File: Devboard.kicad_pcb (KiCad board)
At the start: 4 copper layers, 33.7 x 50.4 mm, 40 parts, among them J1 USB_C_Receptacle_USB2.0_14P, J2 Conn_01x03, J3 Conn_01x10, J4 Conn_01x10, J5 JST_2mm_LiPo, J6 Conn_01x10, J7 Conn_01x10, SW1 SW_Push, U1 RP2040, U2 NCP1117-3.3_SOT223, U3 W25Q128JVS, U4 MPU-9250, Y1 12Mhz

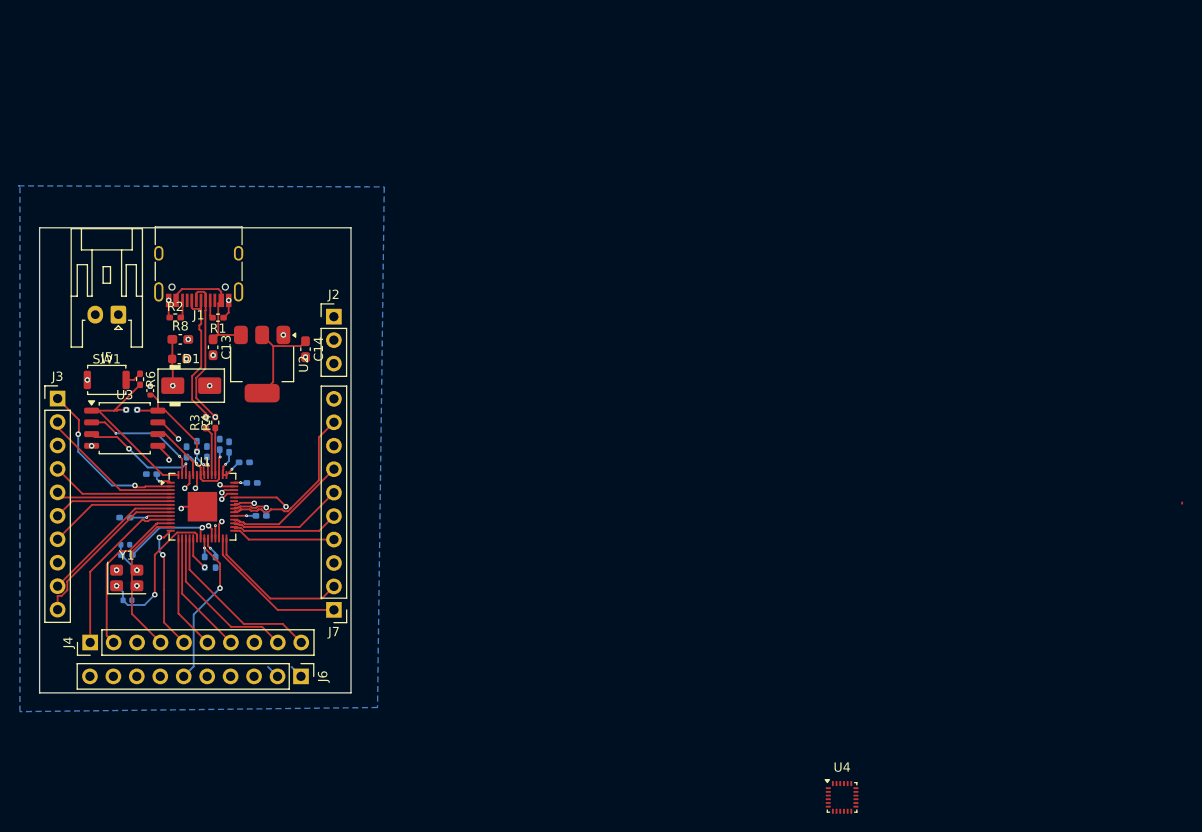
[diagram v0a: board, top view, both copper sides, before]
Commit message: Added an IMU, Solved all DRC thermal relief errors + routed IMU
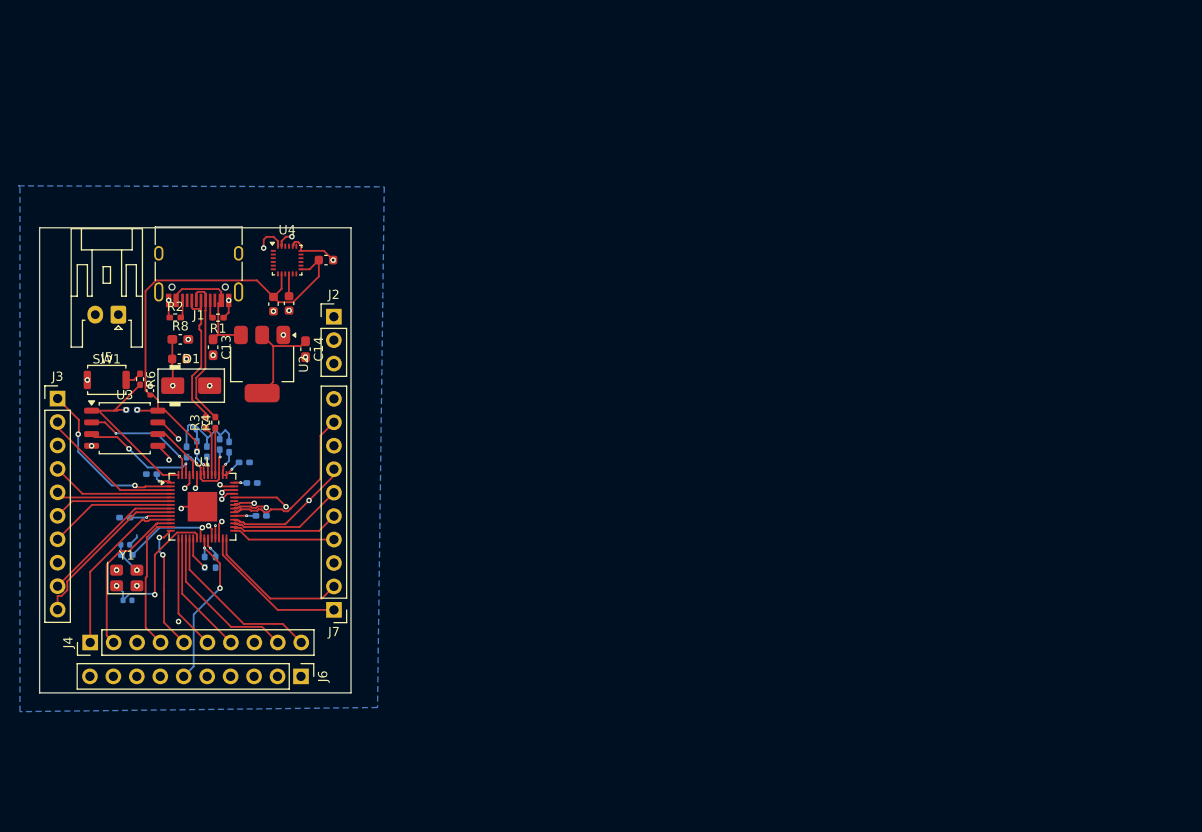
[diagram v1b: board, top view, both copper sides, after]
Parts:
- added C19: 0.1uF, PCM_SparkFun-Capacitor:C_0603_1608Metric, F.Cu at (124.7, 89.3)
- added C20: 0.1uF, PCM_SparkFun-Capacitor:C_0603_1608Metric, F.Cu at (130.4, 84.6)
- added C21: 0.1uF, PCM_SparkFun-Capacitor:C_0603_1608Metric, F.Cu at (126.4, 89.3)
- moved U4 83.7 mm to (126.2, 84.6)
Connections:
- J7 pad 7: /GPIO21 -> /SDA
- J7 pad 9: /GPIO22 -> /SCL
- U1 pad 32: /GPIO21 -> /SDA
- U1 pad 34: /GPIO22 -> /SCL
- U4 pad 10: unconnected-(U4-REGOUT-Pad10) -> Net-(U4-REGOUT)
- U4 pad 13: Net-(U4-VDD) -> +3.3V
- U4 pad 18: unconnected-(U4-GND-Pad18) -> GND
- U4 pad 20: unconnected-(U4-RESV_GND-Pad20) -> GND
- U4 pad 23: unconnected-(U4-SCL/SCLK-Pad23) -> /SCL
- U4 pad 24: unconnected-(U4-SDA/MOSI-Pad24) -> /SDA
- U4 pad 8: Net-(U4-VDD) -> +3.3V
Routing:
- net /SDA: track 0.00 -> 49.2 mm, vias 0 -> 2
- net +3.3V: track 50.3 -> 96.8 mm, vias 12 -> 13
- net /SCL: track 0.00 -> 42.3 mm, vias 0 -> 1
- net GND: track 10.0 -> 32.5 mm, vias 14 -> 17
- net /GPIO22: track 18.1 -> 0.00 mm
- net /GPIO21: track 13.5 -> 0.00 mm
- net Net-(U4-REGOUT): track 0.00 -> 2.42 mm
- net /GPIO24: track 23.7 -> 22.3 mm
- net /GPIO23: track 25.1 -> 23.7 mm
- net /GPIO10: track 16.4 -> 15.2 mm
- net USB_D-: vias 1 -> 0
- net USB_D+: vias 1 -> 0
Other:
- board text added: "Component"
- board text added: "KEEPOUT"
- board text added: "No Copper"

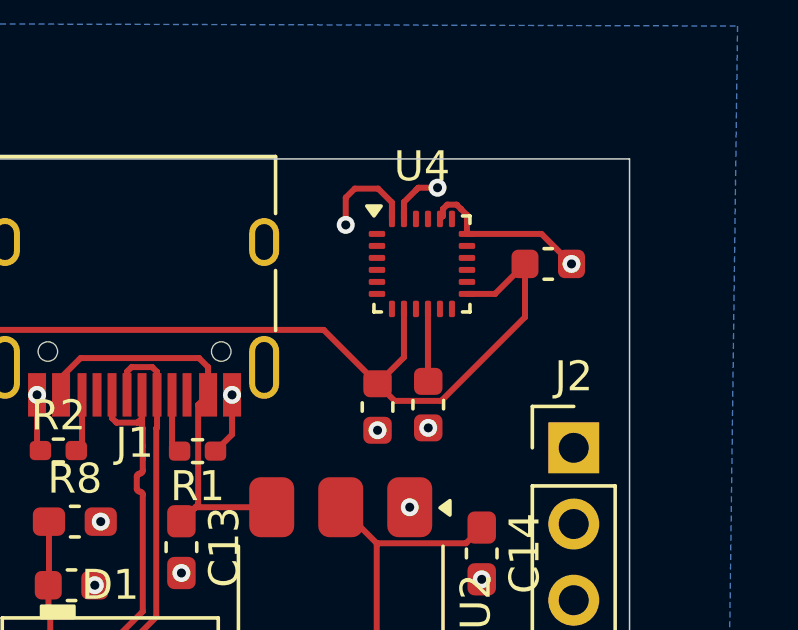
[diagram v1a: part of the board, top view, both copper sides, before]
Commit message: Changed IMU from MPU-6500 to ICM-20948
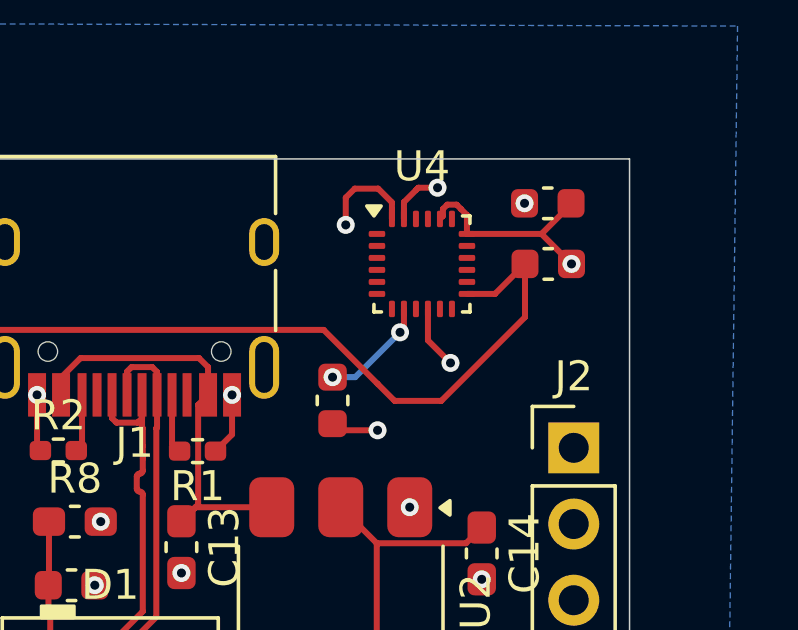
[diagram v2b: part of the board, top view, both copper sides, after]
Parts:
- removed C21: 0.1uF, PCM_SparkFun-Capacitor:C_0603_1608Metric
- added C22: 0.1uF, PCM_SparkFun-Capacitor:C_0603_1608Metric, F.Cu at (130.4, 82.5)
- U4: value MPU-9250 -> ICM-20948
- moved C19 1.52 mm to (123.2, 89.1)
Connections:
- C19 pad 2: +3.3V -> 1.8V
- U4 pad 14: (no net) -> unconnected-(U4-NC-Pad14)
- U4 pad 15: (no net) -> unconnected-(U4-NC-Pad15)
- U4 pad 16: (no net) -> unconnected-(U4-NC-Pad16)
- U4 pad 17: (no net) -> unconnected-(U4-NC-Pad17)
- U4 pad 19: (no net) -> unconnected-(U4-RESV-Pad19)
- U4 pad 2: (no net) -> unconnected-(U4-NC-Pad2)
- U4 pad 3: (no net) -> unconnected-(U4-NC-Pad3)
- U4 pad 4: (no net) -> unconnected-(U4-NC-Pad4)
- U4 pad 5: (no net) -> unconnected-(U4-NC-Pad5)
- U4 pad 6: (no net) -> unconnected-(U4-NC-Pad6)
- U4 pad 8: +3.3V -> 1.8V
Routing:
- net Net-(U4-REGOUT): track 2.42 -> 8.98 mm, vias 0 -> 2
- net 1.8V: track 0.00 -> 3.70 mm, vias 0 -> 2
- net GND: track 32.5 -> 35.6 mm, vias 17 -> 16
- net +3.3V: track 96.8 -> 93.9 mm

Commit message: Updated Devboard
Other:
- board text added: "By Naytik"
- board text added: "RoboBoard V1"
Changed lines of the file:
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@@
 		(layer "Edge.Cuts")
 	)
+	(gr_text "RoboBoard V1"
+		(at 112.7 121.04 0)
+		(layer "F.SilkS")
+		(effects
+			(font
+				(size 1.5 1.5)
+				(thickness 0.3)
+				(bold yes)
+			)
+			(justify left bottom)
+		)
+	)
+	(gr_text "By Naytik"
+		(at 112.95 121.99 0)
+		(layer "F.SilkS")
+		(effects
+			(font
+				(size 0.5 0.5)
+				(thickness 0.1)
+				(bold yes)
+			)
+			(justify left bottom)
+		)
+	)
 	(gr_text "Component"
 		(at 126.21 85.12 0)
@@
 		(polygon
 			(pts
-				(xy 95.49 74.16) (xy 138.23 74.35) (xy 137.73 134.85) (xy 95.74 135.59) (xy 95.86 74.04)
+				(xy 95.49 74.16) (xy 138.23 74.35) (xy 137.73 134.85) (xy 95.96 134.93) (xy 95.86 74.04)
 			)
 		)

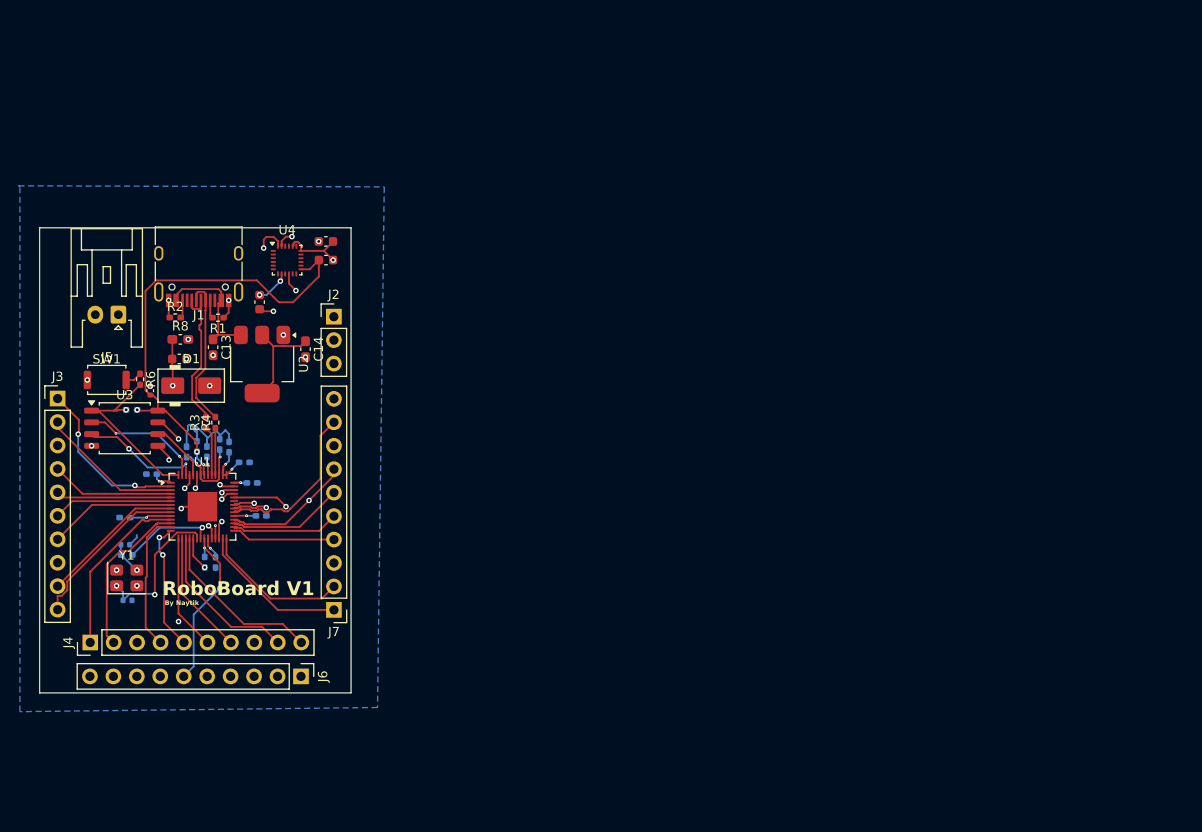
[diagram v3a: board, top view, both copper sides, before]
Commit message: Re-routed the board to a 2-layer PCB and removed IMU unit
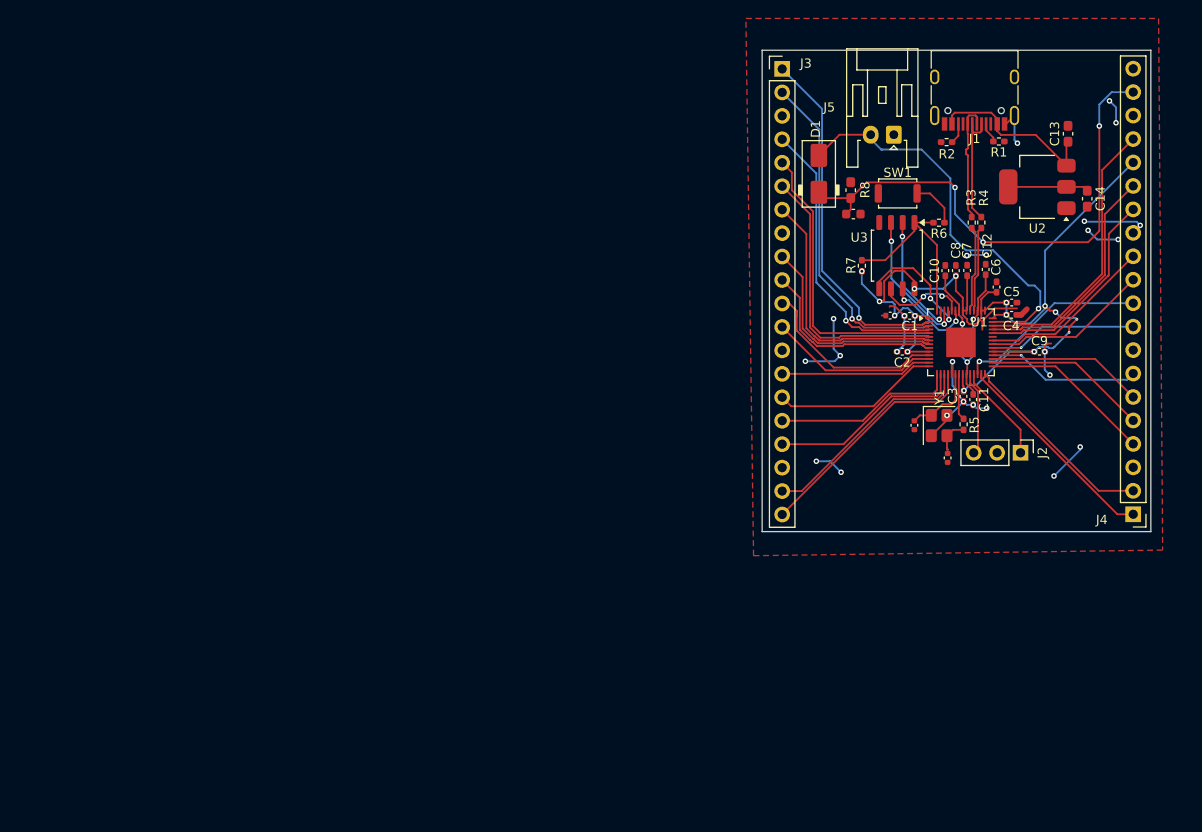
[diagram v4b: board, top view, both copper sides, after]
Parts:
- removed C19, C20, C22: 0.1uF, PCM_SparkFun-Capacitor:C_0603_1608Metric
- removed J6, J7: Conn_01x10, Connector_PinHeader_2.54mm:PinHeader_1x10_P2.54mm_Vertical
- removed U4: ICM-20948, Sensor_Motion:InvenSense_QFN-24_3x3mm_P0.4mm
- C1, C10, C11, C12, C15, C16, C2, C3, C4, C5, C6, C7, C8, C9, R5, R7: moved to F.Cu
- J3, J4: value Conn_01x10 -> Conn_01x20; footprint Connector_PinHeader_2.54mm:PinHeader_1x10_P2.54mm_Vertical -> Connector_PinHeader_2.54mm:PinHeader_1x20_P2.54mm_Vertical
- moved J4 113.8 mm to (217.8, 112.1), turned to 180 degrees
- moved C13 95.4 mm to (210.8, 70.9), turned to 90 degrees
- moved C4 94.7 mm to (204.7, 90.5), turned to 0 degrees
- moved C8 93.9 mm to (198.6, 85.7), turned to 90 degrees
- moved R5 91.7 mm to (199.5, 102.4), turned to 90 degrees
- moved C16 89.6 mm to (197.8, 106.0), turned to 90 degrees
- moved Y1 89.5 mm to (196.8, 102.5), turned to -90 degrees
- moved R6 88.2 mm to (196.8, 80.5), turned to 180 degrees
- moved SW1 88.0 mm to (192.3, 77.3)
- moved C15 87.3 mm to (194.2, 102.5), turned to 90 degrees
- moved R1 86.7 mm to (203.3, 71.7)
- moved C14 86.2 mm to (212.9, 77.9)
- moved J5 86.2 mm to (191.9, 71.0)
- moved J3 86.2 mm to (179.8, 63.9)
- moved J1 86.2 mm to (200.7, 65.8)
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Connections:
- J4 pad 1: /GPIO8 -> /GPIO16
- J4 pad 10: /GPIO15 -> RUN
- J4 pad 2: /GPIO9 -> /GPIO17
- J4 pad 4: /GPIO10 -> /GPIO18
- J4 pad 5: /GPIO11 -> /GPIO19
- J4 pad 6: /GPIO12 -> /GPIO20
- J4 pad 7: /GPIO13 -> /GPIO21
- J4 pad 9: /GPIO14 -> /GPIO22
- U1 pad 32: /SDA -> /GPIO21
- U1 pad 34: /SCL -> /GPIO22
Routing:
- net /SDA: track 49.2 -> 0.00 mm, vias 2 -> 0
- net /SCL: track 42.3 -> 0.00 mm, vias 1 -> 0
- net GND: track 35.6 -> 67.1 mm, vias 16 -> 25
- net SWD: track 32.1 -> 10.6 mm, vias 1 -> 0
- net /GPIO1: track 15.6 -> 36.5 mm, vias 0 -> 1
- net /GPIO0: track 18.4 -> 38.5 mm, vias 2 -> 1
- net /GPIO3: track 12.5 -> 32.0 mm
- net /GPIO2: track 13.4 -> 32.0 mm, vias 0 -> 1
- net /GPIO4: track 12.9 -> 30.0 mm
- net Net-(D1-K): track 39.2 -> 56.1 mm, vias 1 -> 3
- net /GPIO21: track 0.00 -> 16.6 mm, vias 0 -> 1
- net /GPIO22: track 0.00 -> 16.2 mm, vias 0 -> 1
- net SWCLK: track 24.7 -> 9.06 mm, vias 1 -> 0
- net /GPIO29_ADC3: track 28.5 -> 43.4 mm, vias 2 -> 1
- net /GPIO5: track 13.8 -> 27.9 mm
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- added copper zone on F.Cu, net GND
- removed copper zone on In1.Cu, net +3.3V
- removed copper zone on B.Cu, net GND
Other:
- board size 33.7 x 50.4 mm -> 42.1 x 52.1 mm
- copper layers 4 -> 2
- board text removed: "By Naytik"
- board text removed: "Component"
- board text removed: "KEEPOUT"
- board text removed: "No Copper"
- board text removed: "RoboBoard V1"
